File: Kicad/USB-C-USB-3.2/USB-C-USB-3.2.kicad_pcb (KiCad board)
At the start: 2 copper layers, 45 x 26 mm, 7 parts, among them J1 Screw_Terminal_01x16, P1 USB_C_Plug

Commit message: Updated files & some images used in the article
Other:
- board text added: "VBUS A8 B5 B3 B2 A11 A10 A7 A6 A3 A2 B11 B10 B5 B8 GND"
- board text removed: "VBUS A5 B5 A7/B7 A6/B6 B10 B11 A3 A2 A10 A11 B3 B2 A8 B8 GND"

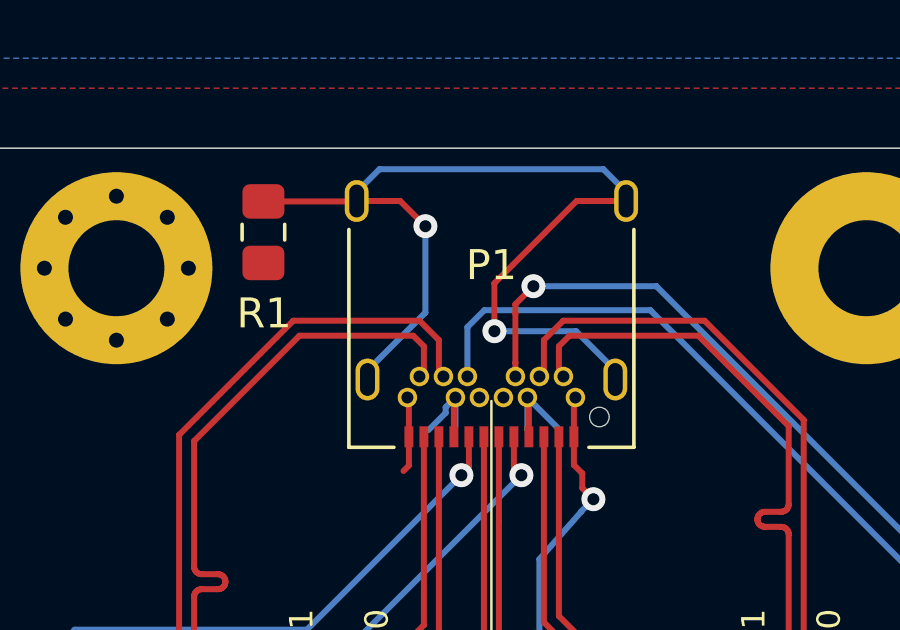
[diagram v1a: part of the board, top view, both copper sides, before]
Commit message: Files and footprint adjusted for error and omission
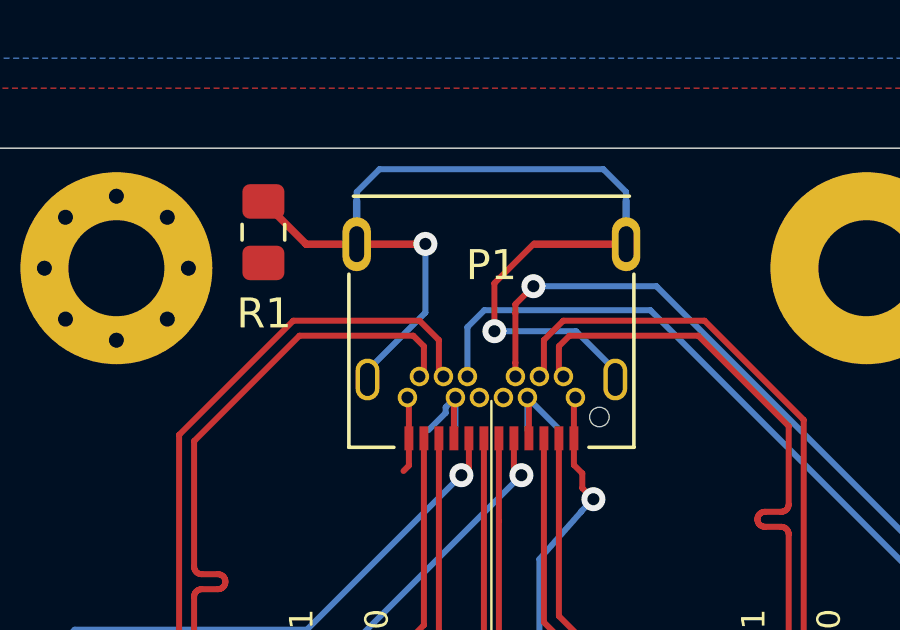
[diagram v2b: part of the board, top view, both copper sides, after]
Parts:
- P1: footprint Connector_USB:USB_C_Receptacle_Amphenol_12401548E4-2A -> USB-C-Power-tester:TYPE-C-31-M-04
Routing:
- net Net-(P1-PadS1): track 33.9 -> 35.8 mm
